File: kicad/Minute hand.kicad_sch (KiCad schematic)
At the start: 66 parts, among them U001 74HC595, U002 74HC595

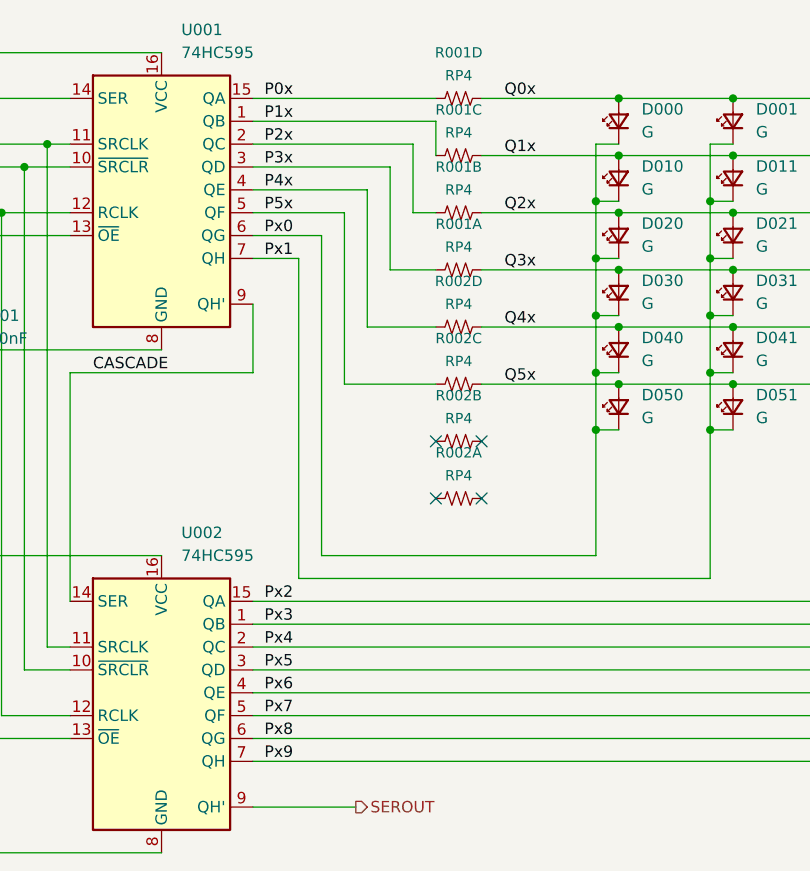
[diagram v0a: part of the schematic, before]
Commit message: Updated to 3 multiplexers
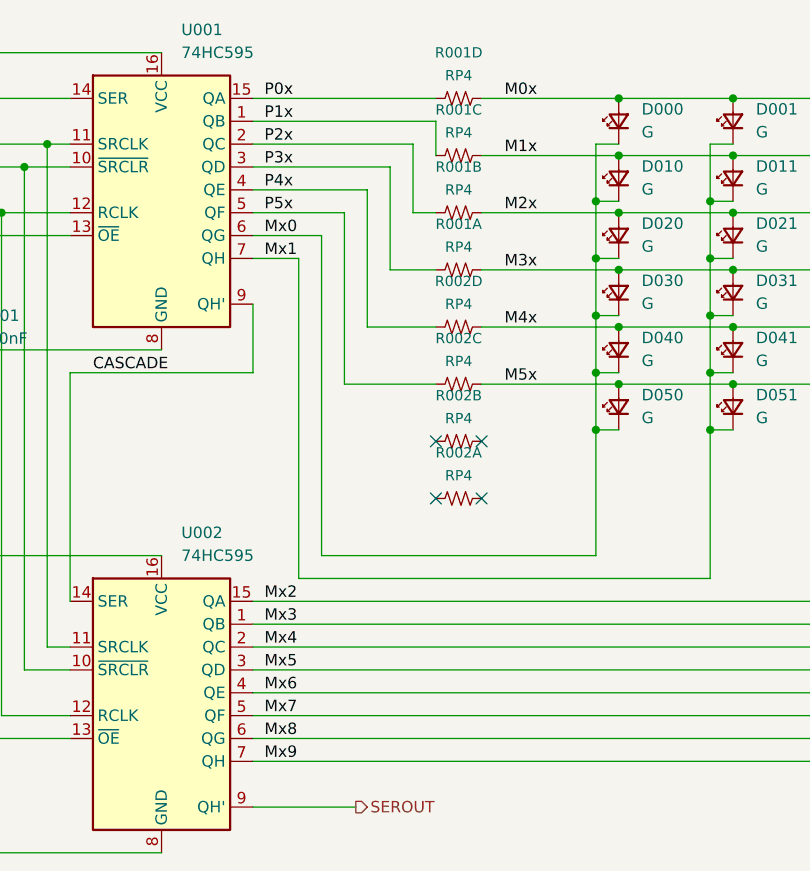
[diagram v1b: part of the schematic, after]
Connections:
- net Px0 renamed Mx0
- net Px1 renamed Mx1
- net Px2 renamed Mx2
- net Px3 renamed Mx3
- net Px4 renamed Mx4
- net Px5 renamed Mx5
- net Px6 renamed Mx6
- net Px7 renamed Mx7
- net Px8 renamed Mx8
- net Px9 renamed Mx9
- net Q0x renamed M0x
- net Q1x renamed M1x
- net Q2x renamed M2x
- net Q3x renamed M3x
- net Q4x renamed M4x
- net Q5x renamed M5x
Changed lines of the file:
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@@
     (stroke (width 0) (type default))
   )
-  (label "Px0" (at 102.87 53.34 0) (fields_autoplaced)
+  (label "Mx0" (at 102.87 53.34 0) (fields_autoplaced)
     (effects (font (size 1.27 1.27)) (justify left bottom))
   )
-  (label "Q4x" (at 129.54 63.5 0) (fields_autoplaced)
+  (label "M4x" (at 129.54 63.5 0) (fields_autoplaced)
     (effects (font (size 1.27 1.27)) (justify left bottom))
   )
-  (label "Px5" (at 102.87 101.6 0) (fields_autoplaced)
+  (label "Mx5" (at 102.87 101.6 0) (fields_autoplaced)
     (effects (font (size 1.27 1.27)) (justify left bottom))
   )
-  (label "Px1" (at 102.87 55.88 0) (fields_autoplaced)
+  (label "Mx1" (at 102.87 55.88 0) (fields_autoplaced)
     (effects (font (size 1.27 1.27)) (justify left bottom))
   )
@@
     (effects (font (size 1.27 1.27)) (justify left bottom))
   )
-  (label "Px3" (at 102.87 96.52 0) (fields_autoplaced)
+  (label "Mx3" (at 102.87 96.52 0) (fields_autoplaced)
     (effects (font (size 1.27 1.27)) (justify left bottom))
   )
@@
     (effects (font (size 1.27 1.27)) (justify left bottom))
   )
-  (label "Q5x" (at 129.54 69.85 0) (fields_autoplaced)
+  (label "M5x" (at 129.54 69.85 0) (fields_autoplaced)
     (effects (font (size 1.27 1.27)) (justify left bottom))
   )
-  (label "Px7" (at 102.87 106.68 0) (fields_autoplaced)
+  (label "Mx7" (at 102.87 106.68 0) (fields_autoplaced)
     (effects (font (size 1.27 1.27)) (justify left bottom))
   )
-  (label "Q2x" (at 129.54 50.8 0) (fields_autoplaced)
+  (label "M2x" (at 129.54 50.8 0) (fields_autoplaced)
     (effects (font (size 1.27 1.27)) (justify left bottom))
   )
-  (label "Q1x" (at 129.54 44.45 0) (fields_autoplaced)
+  (label "M1x" (at 129.54 44.45 0) (fields_autoplaced)
     (effects (font (size 1.27 1.27)) (justify left bottom))
   )
-  (label "Px8" (at 102.87 109.22 0) (fields_autoplaced)
+  (label "Mx8" (at 102.87 109.22 0) (fields_autoplaced)
     (effects (font (size 1.27 1.27)) (justify left bottom))
   )
@@
     (effects (font (size 1.27 1.27)) (justify left bottom))
   )
-  (label "Px6" (at 102.87 104.14 0) (fields_autoplaced)
+  (label "Mx6" (at 102.87 104.14 0) (fields_autoplaced)
     (effects (font (size 1.27 1.27)) (justify left bottom))
   )
@@
     (effects (font (size 1.27 1.27)) (justify left bottom))
   )
-  (label "Q3x" (at 129.54 57.15 0) (fields_autoplaced)
+  (label "M3x" (at 129.54 57.15 0) (fields_autoplaced)
     (effects (font (size 1.27 1.27)) (justify left bottom))
   )
@@
     (effects (font (size 1.27 1.27)) (justify left bottom))
   )
-  (label "Q0x" (at 129.54 38.1 0) (fields_autoplaced)
+  (label "M0x" (at 129.54 38.1 0) (fields_autoplaced)
     (effects (font (size 1.27 1.27)) (justify left bottom))
   )
-  (label "Px9" (at 102.87 111.76 0) (fields_autoplaced)
+  (label "Mx9" (at 102.87 111.76 0) (fields_autoplaced)
     (effects (font (size 1.27 1.27)) (justify left bottom))
   )
-  (label "Px4" (at 102.87 99.06 0) (fields_autoplaced)
+  (label "Mx4" (at 102.87 99.06 0) (fields_autoplaced)
     (effects (font (size 1.27 1.27)) (justify left bottom))
   )
-  (label "Px2" (at 102.87 93.98 0) (fields_autoplaced)
+  (label "Mx2" (at 102.87 93.98 0) (fields_autoplaced)
     (effects (font (size 1.27 1.27)) (justify left bottom))
   )

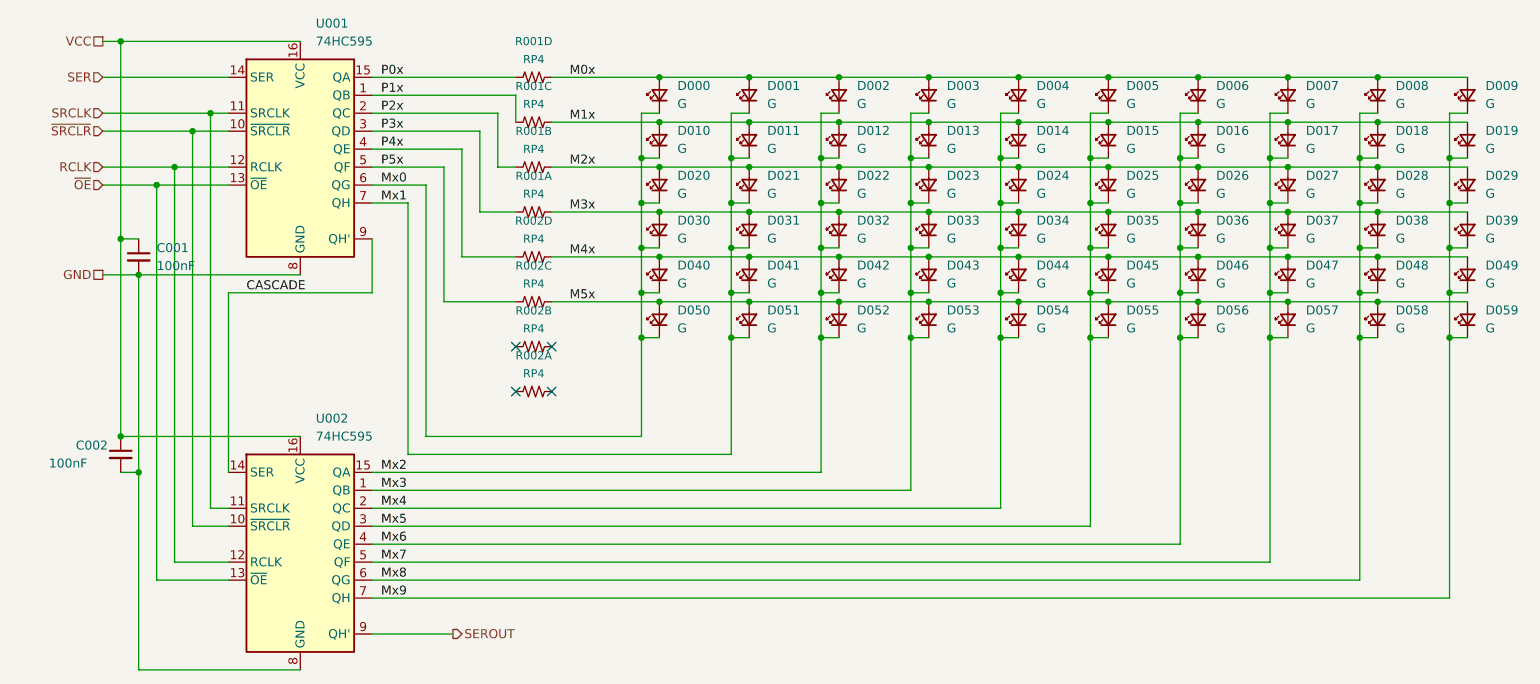
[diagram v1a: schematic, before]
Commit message: Add notes for diode voltages
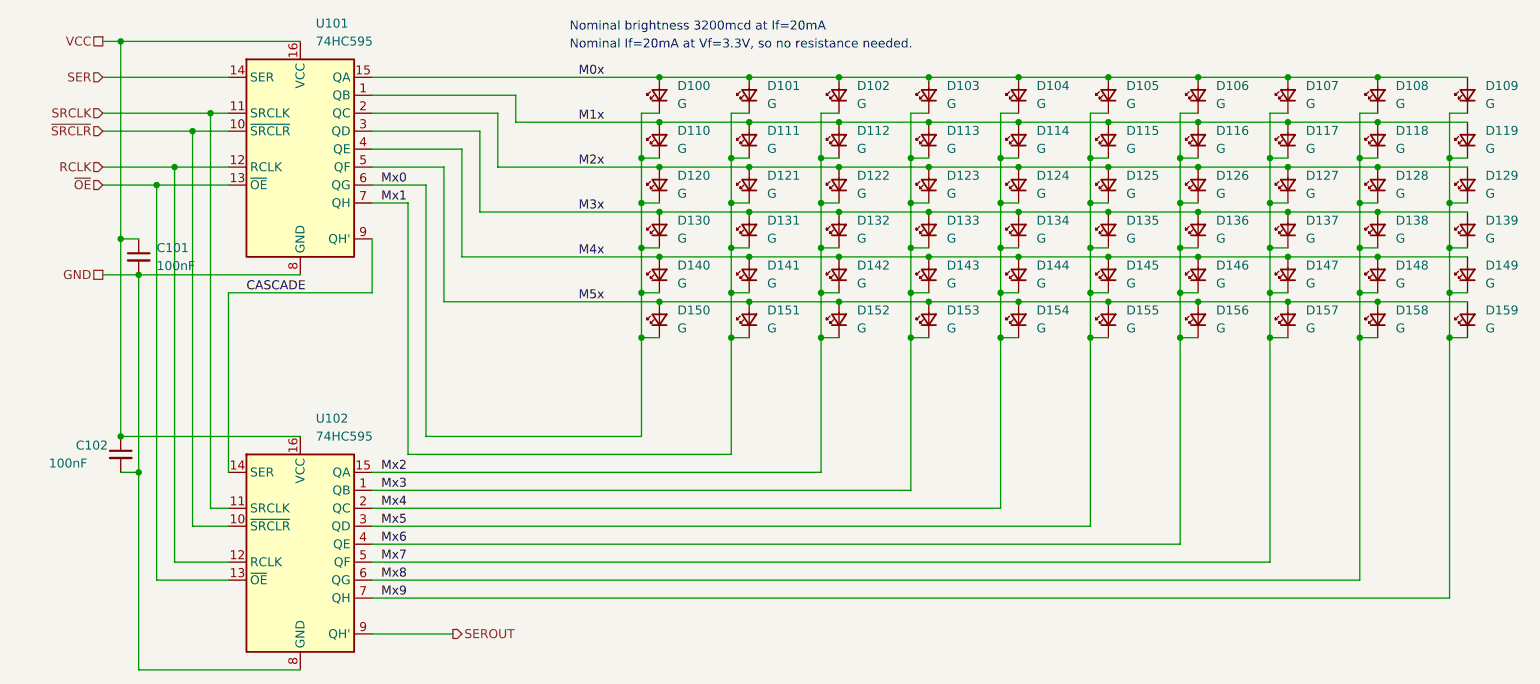
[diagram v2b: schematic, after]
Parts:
- removed R001, R002: RP4, KwanSystems:R_Array_Convex_4x0402, symbol KwanSystems:RP4
- C101: renamed from C001; Digikey (none) -> 445-5613-1-ND; Part Number (none) -> CGA2B1X7R1C104K050BC; Purpose (none) -> Minute hand decoder bypass
- C102: renamed from C002; Digikey (none) -> 445-5613-1-ND; Part Number (none) -> CGA2B1X7R1C104K050BC; Purpose (none) -> Minute hand decoder bypass
- D100: renamed from D000; Digikey 754-2337-1-ND -> 754-2334-1-ND; Part Number APDA1806CGCK -> APDA1806ZGCK; Purpose (none) -> Green minute hand
- D101: renamed from D001; Digikey 754-2337-1-ND -> 754-2334-1-ND; Part Number APDA1806CGCK -> APDA1806ZGCK; Purpose (none) -> Green minute hand
- D102: renamed from D002; Digikey 754-2337-1-ND -> 754-2334-1-ND; Part Number APDA1806CGCK -> APDA1806ZGCK; Purpose (none) -> Green minute hand
- D103: renamed from D003; Digikey 754-2337-1-ND -> 754-2334-1-ND; Part Number APDA1806CGCK -> APDA1806ZGCK; Purpose (none) -> Green minute hand
- D104: renamed from D004; Digikey 754-2337-1-ND -> 754-2334-1-ND; Part Number APDA1806CGCK -> APDA1806ZGCK; Purpose (none) -> Green minute hand
- D105: renamed from D005; Digikey 754-2337-1-ND -> 754-2334-1-ND; Part Number APDA1806CGCK -> APDA1806ZGCK; Purpose (none) -> Green minute hand
- D106: renamed from D006; Digikey 754-2337-1-ND -> 754-2334-1-ND; Part Number APDA1806CGCK -> APDA1806ZGCK; Purpose (none) -> Green minute hand
- D107: renamed from D007; Digikey 754-2337-1-ND -> 754-2334-1-ND; Part Number APDA1806CGCK -> APDA1806ZGCK; Purpose (none) -> Green minute hand
- D108: renamed from D008; Digikey 754-2337-1-ND -> 754-2334-1-ND; Part Number APDA1806CGCK -> APDA1806ZGCK; Purpose (none) -> Green minute hand
- D109: renamed from D009; Digikey 754-2337-1-ND -> 754-2334-1-ND; Part Number APDA1806CGCK -> APDA1806ZGCK; Purpose (none) -> Green minute hand
- D110: renamed from D010; Digikey 754-2337-1-ND -> 754-2334-1-ND; Part Number APDA1806CGCK -> APDA1806ZGCK; Purpose (none) -> Green minute hand
- D111: renamed from D011; Digikey 754-2337-1-ND -> 754-2334-1-ND; Part Number APDA1806CGCK -> APDA1806ZGCK; Purpose (none) -> Green minute hand
- D112: renamed from D012; Digikey 754-2337-1-ND -> 754-2334-1-ND; Part Number APDA1806CGCK -> APDA1806ZGCK; Purpose (none) -> Green minute hand
- D113: renamed from D013; Digikey 754-2337-1-ND -> 754-2334-1-ND; Part Number APDA1806CGCK -> APDA1806ZGCK; Purpose (none) -> Green minute hand
- D114: renamed from D014; Digikey 754-2337-1-ND -> 754-2334-1-ND; Part Number APDA1806CGCK -> APDA1806ZGCK; Purpose (none) -> Green minute hand
- D115: renamed from D015; Digikey 754-2337-1-ND -> 754-2334-1-ND; Part Number APDA1806CGCK -> APDA1806ZGCK; Purpose (none) -> Green minute hand
- D116: renamed from D016; Digikey 754-2337-1-ND -> 754-2334-1-ND; Part Number APDA1806CGCK -> APDA1806ZGCK; Purpose (none) -> Green minute hand
- D117: renamed from D017; Digikey 754-2337-1-ND -> 754-2334-1-ND; Part Number APDA1806CGCK -> APDA1806ZGCK; Purpose (none) -> Green minute hand
- D118: renamed from D018; Digikey 754-2337-1-ND -> 754-2334-1-ND; Part Number APDA1806CGCK -> APDA1806ZGCK; Purpose (none) -> Green minute hand
- D119: renamed from D019; Digikey 754-2337-1-ND -> 754-2334-1-ND; Part Number APDA1806CGCK -> APDA1806ZGCK; Purpose (none) -> Green minute hand
- D120: renamed from D020; Digikey 754-2337-1-ND -> 754-2334-1-ND; Part Number APDA1806CGCK -> APDA1806ZGCK; Purpose (none) -> Green minute hand
- D121: renamed from D021; Digikey 754-2337-1-ND -> 754-2334-1-ND; Part Number APDA1806CGCK -> APDA1806ZGCK; Purpose (none) -> Green minute hand
- D122: renamed from D022; Digikey 754-2337-1-ND -> 754-2334-1-ND; Part Number APDA1806CGCK -> APDA1806ZGCK; Purpose (none) -> Green minute hand
- D123: renamed from D023; Digikey 754-2337-1-ND -> 754-2334-1-ND; Part Number APDA1806CGCK -> APDA1806ZGCK; Purpose (none) -> Green minute hand
- D124: renamed from D024; Digikey 754-2337-1-ND -> 754-2334-1-ND; Part Number APDA1806CGCK -> APDA1806ZGCK; Purpose (none) -> Green minute hand
- D125: renamed from D025; Digikey 754-2337-1-ND -> 754-2334-1-ND; Part Number APDA1806CGCK -> APDA1806ZGCK; Purpose (none) -> Green minute hand
- D126: renamed from D026; Digikey 754-2337-1-ND -> 754-2334-1-ND; Part Number APDA1806CGCK -> APDA1806ZGCK; Purpose (none) -> Green minute hand
- D127: renamed from D027; Digikey 754-2337-1-ND -> 754-2334-1-ND; Part Number APDA1806CGCK -> APDA1806ZGCK; Purpose (none) -> Green minute hand
- D128: renamed from D028; Digikey 754-2337-1-ND -> 754-2334-1-ND; Part Number APDA1806CGCK -> APDA1806ZGCK; Purpose (none) -> Green minute hand
- D129: renamed from D029; Digikey 754-2337-1-ND -> 754-2334-1-ND; Part Number APDA1806CGCK -> APDA1806ZGCK; Purpose (none) -> Green minute hand
- D130: renamed from D030; Digikey 754-2337-1-ND -> 754-2334-1-ND; Part Number APDA1806CGCK -> APDA1806ZGCK; Purpose (none) -> Green minute hand
- D131: renamed from D031; Digikey 754-2337-1-ND -> 754-2334-1-ND; Part Number APDA1806CGCK -> APDA1806ZGCK; Purpose (none) -> Green minute hand
- D132: renamed from D032; Digikey 754-2337-1-ND -> 754-2334-1-ND; Part Number APDA1806CGCK -> APDA1806ZGCK; Purpose (none) -> Green minute hand
- D133: renamed from D033; Digikey 754-2337-1-ND -> 754-2334-1-ND; Part Number APDA1806CGCK -> APDA1806ZGCK; Purpose (none) -> Green minute hand
- D134: renamed from D034; Digikey 754-2337-1-ND -> 754-2334-1-ND; Part Number APDA1806CGCK -> APDA1806ZGCK; Purpose (none) -> Green minute hand
- D135: renamed from D035; Digikey 754-2337-1-ND -> 754-2334-1-ND; Part Number APDA1806CGCK -> APDA1806ZGCK; Purpose (none) -> Green minute hand
- D136: renamed from D036; Digikey 754-2337-1-ND -> 754-2334-1-ND; Part Number APDA1806CGCK -> APDA1806ZGCK; Purpose (none) -> Green minute hand
- D137: renamed from D037; Digikey 754-2337-1-ND -> 754-2334-1-ND; Part Number APDA1806CGCK -> APDA1806ZGCK; Purpose (none) -> Green minute hand
- D138: renamed from D038; Digikey 754-2337-1-ND -> 754-2334-1-ND; Part Number APDA1806CGCK -> APDA1806ZGCK; Purpose (none) -> Green minute hand
- D139: renamed from D039; Digikey 754-2337-1-ND -> 754-2334-1-ND; Part Number APDA1806CGCK -> APDA1806ZGCK; Purpose (none) -> Green minute hand
- D140: renamed from D040; Digikey 754-2337-1-ND -> 754-2334-1-ND; Part Number APDA1806CGCK -> APDA1806ZGCK; Purpose (none) -> Green minute hand
- D141: renamed from D041; Digikey 754-2337-1-ND -> 754-2334-1-ND; Part Number APDA1806CGCK -> APDA1806ZGCK; Purpose (none) -> Green minute hand
- D142: renamed from D042; Digikey 754-2337-1-ND -> 754-2334-1-ND; Part Number APDA1806CGCK -> APDA1806ZGCK; Purpose (none) -> Green minute hand
- D143: renamed from D043; Digikey 754-2337-1-ND -> 754-2334-1-ND; Part Number APDA1806CGCK -> APDA1806ZGCK; Purpose (none) -> Green minute hand
- D144: renamed from D044; Digikey 754-2337-1-ND -> 754-2334-1-ND; Part Number APDA1806CGCK -> APDA1806ZGCK; Purpose (none) -> Green minute hand
- D145: renamed from D045; Digikey 754-2337-1-ND -> 754-2334-1-ND; Part Number APDA1806CGCK -> APDA1806ZGCK; Purpose (none) -> Green minute hand
- D146: renamed from D046; Digikey 754-2337-1-ND -> 754-2334-1-ND; Part Number APDA1806CGCK -> APDA1806ZGCK; Purpose (none) -> Green minute hand
- D147: renamed from D047; Digikey 754-2337-1-ND -> 754-2334-1-ND; Part Number APDA1806CGCK -> APDA1806ZGCK; Purpose (none) -> Green minute hand
- D148: renamed from D048; Digikey 754-2337-1-ND -> 754-2334-1-ND; Part Number APDA1806CGCK -> APDA1806ZGCK; Purpose (none) -> Green minute hand
- D149: renamed from D049; Digikey 754-2337-1-ND -> 754-2334-1-ND; Part Number APDA1806CGCK -> APDA1806ZGCK; Purpose (none) -> Green minute hand
- D150: renamed from D050; Digikey 754-2337-1-ND -> 754-2334-1-ND; Part Number APDA1806CGCK -> APDA1806ZGCK; Purpose (none) -> Green minute hand
- D151: renamed from D051; Digikey 754-2337-1-ND -> 754-2334-1-ND; Part Number APDA1806CGCK -> APDA1806ZGCK; Purpose (none) -> Green minute hand
- D152: renamed from D052; Digikey 754-2337-1-ND -> 754-2334-1-ND; Part Number APDA1806CGCK -> APDA1806ZGCK; Purpose (none) -> Green minute hand
- D153: renamed from D053; Digikey 754-2337-1-ND -> 754-2334-1-ND; Part Number APDA1806CGCK -> APDA1806ZGCK; Purpose (none) -> Green minute hand
- D154: renamed from D054; Digikey 754-2337-1-ND -> 754-2334-1-ND; Part Number APDA1806CGCK -> APDA1806ZGCK; Purpose (none) -> Green minute hand
- D155: renamed from D055; Digikey 754-2337-1-ND -> 754-2334-1-ND; Part Number APDA1806CGCK -> APDA1806ZGCK; Purpose (none) -> Green minute hand
- D156: renamed from D056; Digikey 754-2337-1-ND -> 754-2334-1-ND; Part Number APDA1806CGCK -> APDA1806ZGCK; Purpose (none) -> Green minute hand
- D157: renamed from D057; Digikey 754-2337-1-ND -> 754-2334-1-ND; Part Number APDA1806CGCK -> APDA1806ZGCK; Purpose (none) -> Green minute hand
- D158: renamed from D058; Digikey 754-2337-1-ND -> 754-2334-1-ND; Part Number APDA1806CGCK -> APDA1806ZGCK; Purpose (none) -> Green minute hand
- D159: renamed from D059; Digikey 754-2337-1-ND -> 754-2334-1-ND; Part Number APDA1806CGCK -> APDA1806ZGCK; Purpose (none) -> Green minute hand
- U101: renamed from U001; Part Number (none) -> 74HC595PW,118; Purpose (none) -> Hand Decoder
- U102: renamed from U002; Part Number (none) -> 74HC595PW,118; Purpose (none) -> Hand Decoder
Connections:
- net P0x is gone; now on net M0x: U101.15 (QA)
- net P1x is gone; now on net M1x: U101.1 (QB)
- net P2x is gone; now on net M2x: U101.2 (QC)
- net P3x is gone; now on net M3x: U101.3 (QD)
- net P4x is gone; now on net M4x: U101.4 (QE)
- net P5x is gone; now on net M5x: U101.5 (QF)
- no-connect marks 4 -> 0
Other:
- note added: "Nominal If=20mA at Vf=3.3V, so no resistance needed."
- note added: "Nominal brightness 3200mcd at If=20mA"

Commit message: Matrix8x8 stuff
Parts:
- removed C101, C102: 100nF, Capacitor_SMD:C_0603_1608Metric, symbol Device:C_Small
- removed D100, D101, D102, D103, D104, D105, D106, D107, D108, D109, D110, D111, D112, D113, D114, D115, D116, D117, D118, D119, D120, D121, D122, D123, D124, D125, D126, D127, D128, D129, D130, D131, D132, D133, D134, D135, D136, D137, D138, D139, D140, D141, D142, D143, D144, D145, D146, D147, D148, D149, D150, D151, D152, D153, D154, D155, D156, D157, D158, D159: G, KwanSystems:D_KINGBRIGHT_DOME, symbol Device:LED_Small
- removed U101, U102: 74HC595, Package_SO:TSSOP-16_4.4x5mm_P0.65mm, symbol 74xx:74HC595
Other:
- note removed: "Nominal If=20mA at Vf=3.3V, so no resistance needed."
- note removed: "Nominal brightness 3200mcd at If=20mA"
